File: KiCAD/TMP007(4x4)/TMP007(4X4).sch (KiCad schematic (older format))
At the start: 16 parts, among them U1 TMP007, U2 TMP007, U3 TMP007, U4 TMP007, U5 TMP007, U6 TMP007, U7 TMP007, U8 TMP007

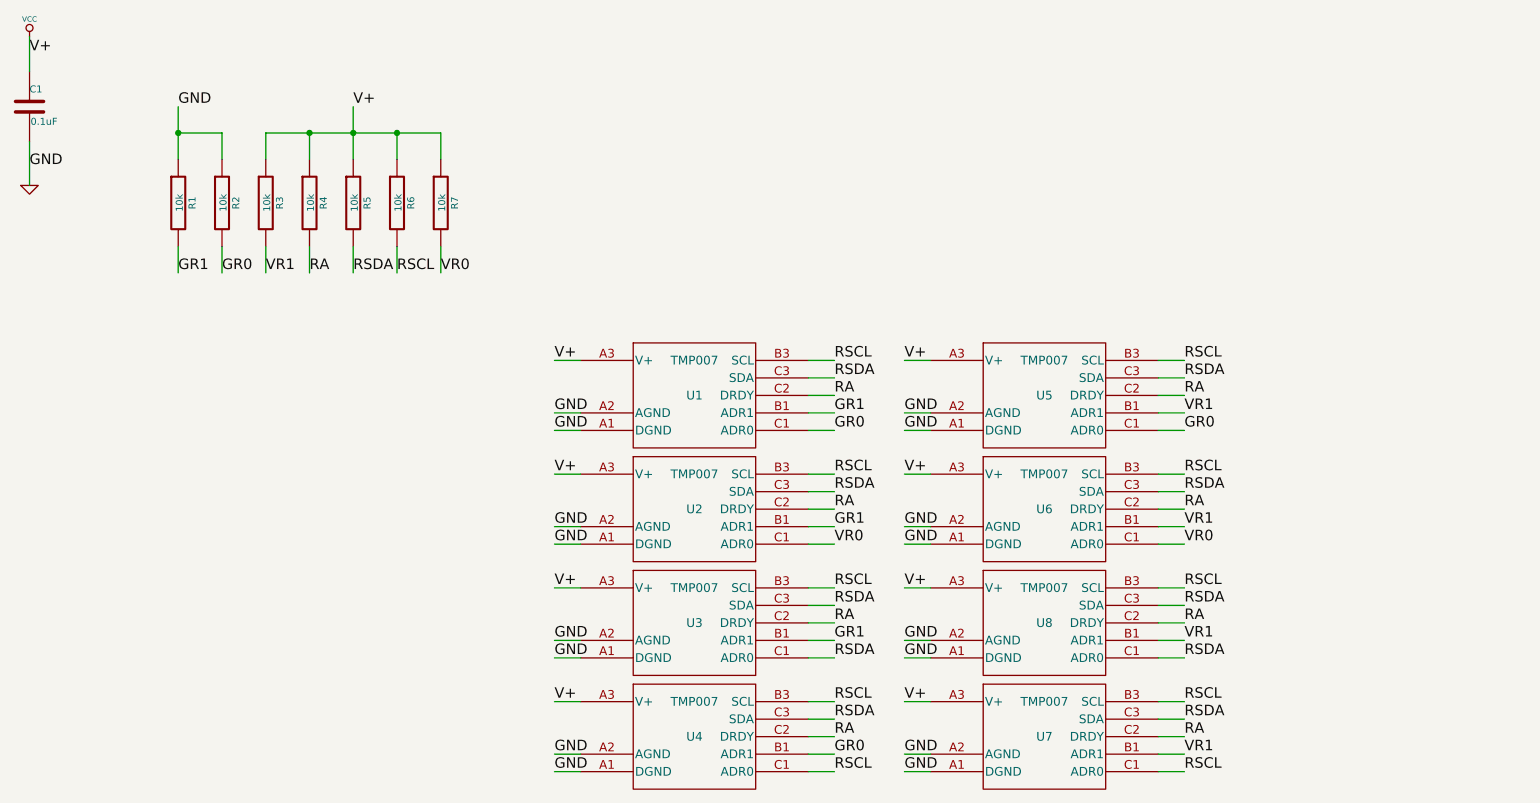
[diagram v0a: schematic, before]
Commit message: Getting Traces Working
Had re do the layout for the IR lens. Trying to get the routing and
traces to work. There may be a problem with the paste layer on the top
layer copper.
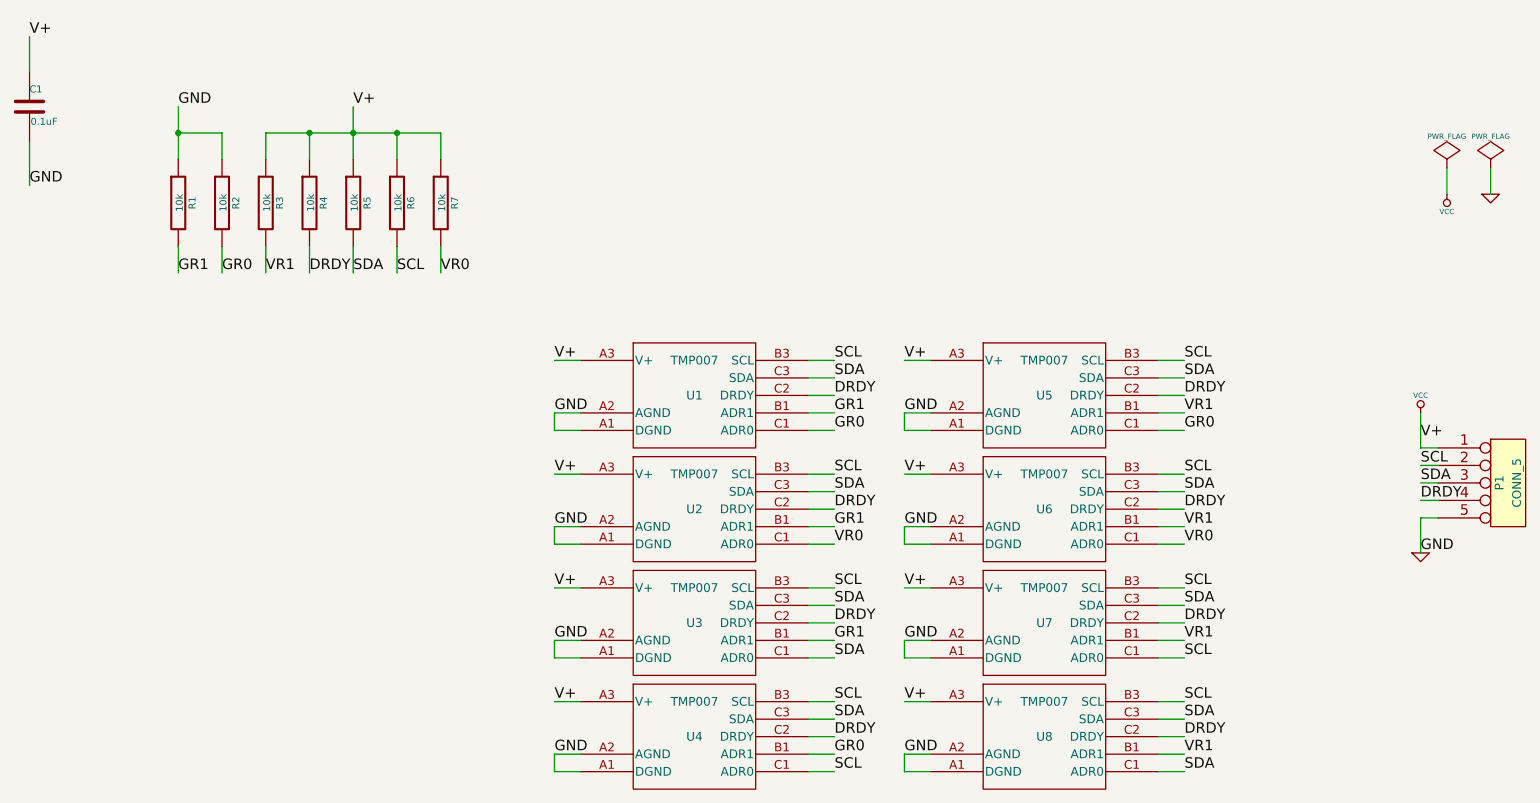
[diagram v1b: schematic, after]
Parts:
- added P1: CONN_5, symbol CONN_5
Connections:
- net GND: now also P1.5
- net VCC: now also P1.1
- net RA renamed DRDY
- net DRDY: now also P1.4
- net RSCL renamed SCL
- net SCL: now also P1.2
- net RSDA renamed SDA
- net SDA: now also P1.3
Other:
- moved on the sheet: U7, U8
